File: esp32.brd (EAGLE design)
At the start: 40.1 x 39.1 mm, 4 parts, among them U1 ESP32MOD

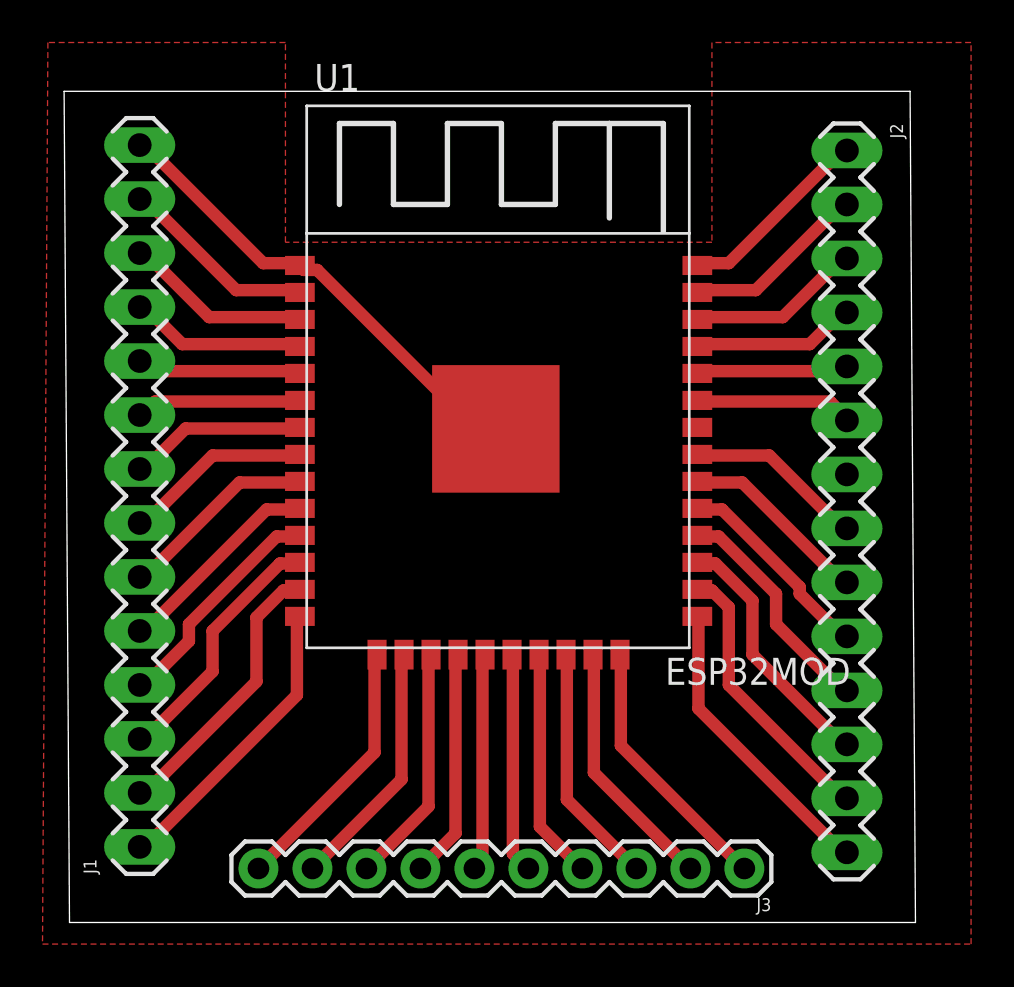
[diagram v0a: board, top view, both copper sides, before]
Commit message: ground clearance between pads increased and GPIO 20 connected
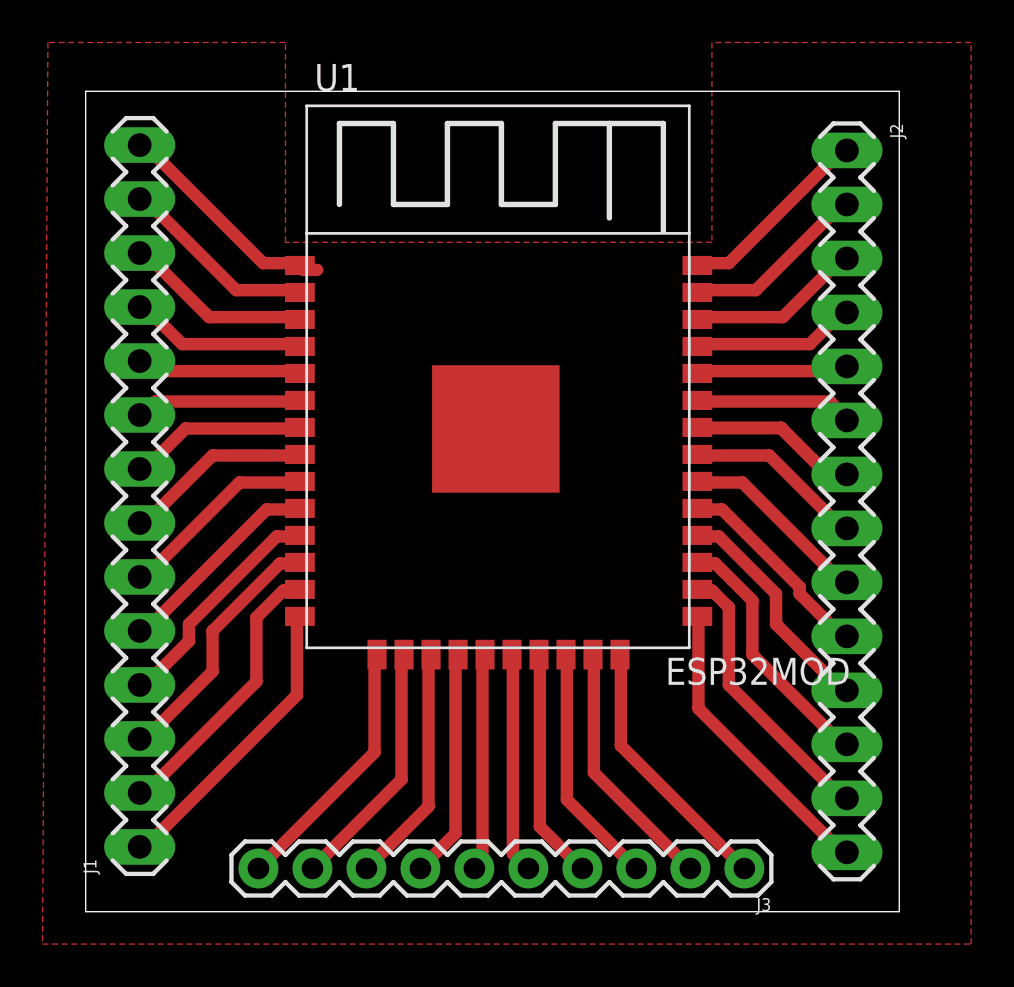
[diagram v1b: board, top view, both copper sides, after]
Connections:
- new net N$1: J2.7, U1.32
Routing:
- net GND: track 44.0 -> 33.4 mm
- net N$1: track 0.00 -> 7.95 mm
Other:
- board size 40.1 x 39.1 mm -> 38.3 x 38.6 mm
